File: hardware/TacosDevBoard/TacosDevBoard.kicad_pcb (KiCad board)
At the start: 2 copper layers, 63.6 x 108.1 mm, 12 parts, among them IC2_COMM1 Conn_01x08_Socket, J1 Conn_01x08_Socket, J2 Conn_01x08_Socket, J3 Conn_01x08_Socket, J4 Conn_01x08_Socket, J5 Conn_01x08_Socket, J6 Micro_SD_Card_Det2, J8 Conn_02x17_Odd_Even, J9 Conn_01x10_Pin

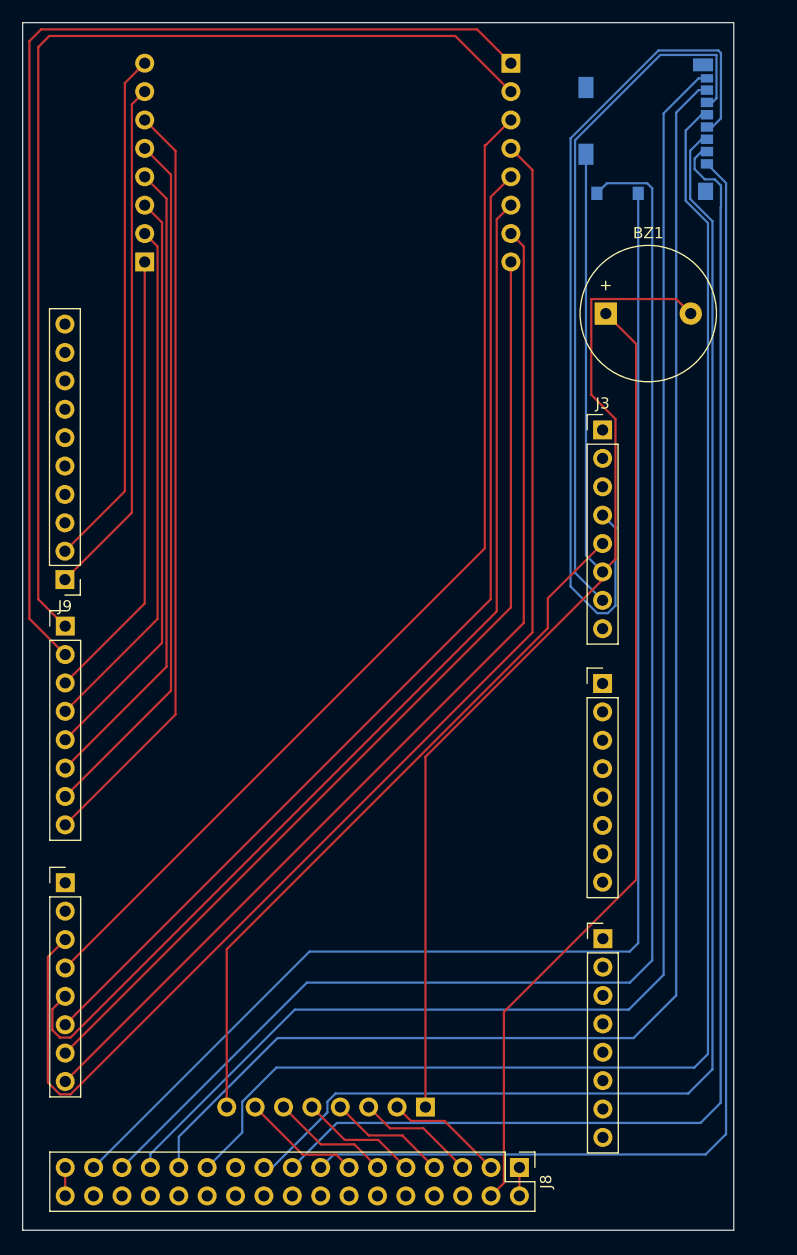
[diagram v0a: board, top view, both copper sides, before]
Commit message: finished dev board rewire
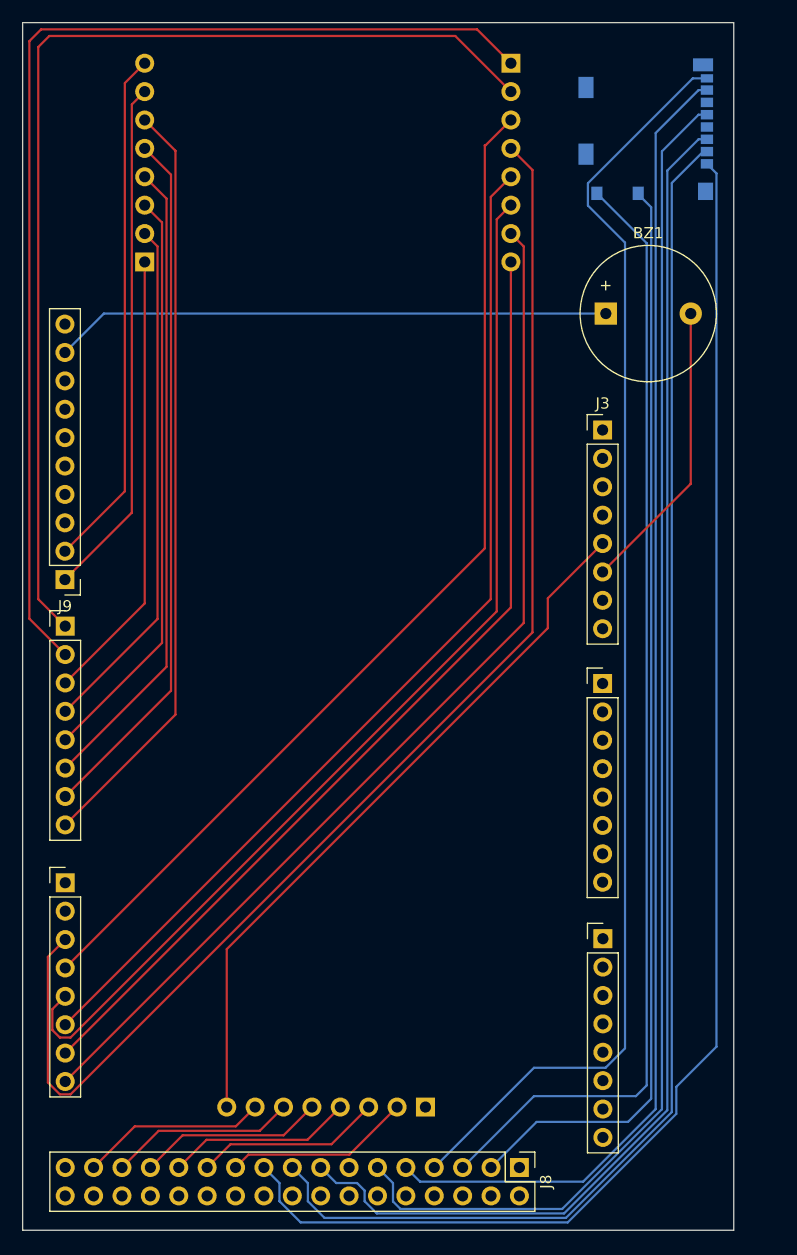
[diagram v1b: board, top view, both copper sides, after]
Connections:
- J8 pad 11: D30 -> SD_CLK
- J8 pad 13: D32 -> unconnected-(J8-Pin_13-Pad13)
- J8 pad 15: SD_DAT2 -> SD_CMD
- J8 pad 19: SD_CMD -> SD_DAT2
- J8 pad 21: unconnected-(J8-Pin_21-Pad21) -> D32
- J8 pad 23: SD_CLK -> D30
- J8 pad 25: SD_DAT0 -> D28
- J8 pad 27: SD_DAT1 -> D26
- J8 pad 29: SD_DET_A -> D24
- J8 pad 3: D22 -> SD_DET_B
- J8 pad 31: SD_DET_B -> D22
- J8 pad 4: D52 -> unconnected-(J8-Pin_4-Pad4)
- J8 pad 5: D24 -> SD_DET_A
- J8 pad 7: D26 -> SD_DAT1
- J8 pad 9: D28 -> SD_DAT0
- J9 pad 9: unconnected-(J9-Pin_9-Pad9) -> D52
- SELECT1 pad 2: D22 -> D32
- SELECT1 pad 3: D24 -> D30
- SELECT1 pad 4: D26 -> D28
- SELECT1 pad 5: D28 -> D26
- SELECT1 pad 6: D30 -> D24
- SELECT1 pad 7: D32 -> D22
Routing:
- net GND: track 130.2 -> 26.4 mm
- net VDD: track 78.2 -> 0.00 mm
- net VSS: track 62.9 -> 0.00 mm
- net D52: track 85.4 -> 49.8 mm
- net SD_DET_A: track 129.7 -> 101.2 mm
- net SD_DET_B: track 124.1 -> 98.4 mm
- net SD_DAT1: track 136.0 -> 114.8 mm
- net SD_DAT0: track 135.1 -> 119.1 mm
- net SD_CLK: track 136.6 -> 122.7 mm
- net D24: track 10.6 -> 16.7 mm
- net D30: track 10.6 -> 16.7 mm
- net D32: track 10.6 -> 16.7 mm
- net D28: track 10.6 -> 16.7 mm
- net D22: track 10.7 -> 16.7 mm
- net D26: track 10.7 -> 16.7 mm
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
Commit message: cleaned up silks
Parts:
- renumbered BZ1 to BZ, IC2_COMM1 to COMM, PWM1 to PWM, SELECT1 to SELECT
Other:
- board text added: "T.A.C.O.S Dev Board"
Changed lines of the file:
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@@
 			(at 0 20.16 0)
 			(layer "F.Fab")
+			(hide yes)
 			(effects
 				(font
@@
 		(descr "Generic Buzzer, D12mm height 9.5mm with RM7.6mm")
 		(tags "buzzer")
-		(property "Reference" "BZ1"
+		(property "Reference" "BZ"
 			(at 3.8 -7.2 0)
 			(layer "F.SilkS")
@@
 			)
 		)
-		(fp_text user "${REFERENCE}"
-			(at 3.8 -4 0)
-			(layer "F.Fab")
-			(effects
-				(font
-					(size 1 1)
-					(thickness 0.15)
-				)
-			)
-		)
 		(pad "1" thru_hole rect
 			(at 0 0)
@@
 			(at 0 -2.38 0)
 			(layer "F.SilkS")
+			(hide yes)
 			(effects
 				(font
@@
 			(at 1.27 -2.38 90)
 			(layer "F.SilkS")
+			(hide yes)
 			(effects
 				(font
@@
 			(at 0 -2.38 0)
 			(layer "F.SilkS")
+			(hide yes)
 			(effects
 				(font
@@
 		(descr "Through hole straight socket strip, 1x08, 2.54mm pitch, single row (from Kicad 4.0.7), script generated")
 		(tags "Through hole socket strip THT 1x08 2.54mm single row")
-		(property "Reference" "PWM1"
-			(at -0.025 -21.336 0)
+		(property "Reference" "PWM"
+			(at 0.0508 -20.3454 0)
 			(layer "B.SilkS")
 			(effects
@@
 		(descr "Through hole straight socket strip, 1x08, 2.54mm pitch, single row (from Kicad 4.0.7), script generated")
 		(tags "Through hole socket strip THT 1x08 2.54mm single row")
-		(property "Reference" "IC2_COMM1"
+		(property "Reference" "COMM"
 			(at 0 2.77 0)
 			(layer "B.SilkS")
@@
 		(descr "Through hole straight socket strip, 1x08, 2.54mm pitch, single row (from Kicad 4.0.7), script generated")
 		(tags "Through hole socket strip THT 1x08 2.54mm single row")
-		(property "Reference" "SELECT1"
+		(property "Reference" "SELECT"
 			(at -2.976 -16.32 0)
 			(layer "B.SilkS")
@@
 		(layer "Edge.Cuts")
 	)
+	(gr_text "T.A.C.O.S Dev Board"
+		(at 157.6832 142.2654 0)
+		(layer "F.SilkS")
+		(effects
+			(font
+				(size 1 1)
+				(thickness 0.1)
+			)
+			(justify left bottom)
+		)
+	)
 	(gr_text "${REFERENCE}"

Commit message: started working on hat detection and selection
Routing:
- net GND: track 26.4 -> 92.3 mm
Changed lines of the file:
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@@
 			(drillshape 0)
 			(scaleselection 1)
-			(outputdirectory "D:/Programming/Aerospace/KiCad/Gerber/")
+			(outputdirectory "DevBoard/")
 		)
 	)
@@
 	)
 	(segment
+		(start 145.2626 131.4958)
+		(end 145.2626 100.1776)
+		(width 0.2)
+		(layer "F.Cu")
+		(net 3)
+	)
+	(segment
+		(start 145.2626 100.1776)
+		(end 161.1122 84.328)
+		(width 0.2)
+		(layer "F.Cu")
+		(net 3)
+	)
+	(segment
 		(start 169 75.729)
 		(end 161.1122 83.6168)
@@
 		(net 3)
 	)
+	(segment
+		(start 161.1122 84.328)
+		(end 161.1122 83.6168)
+		(width 0.2)
+		(layer "F.Cu")
+		(net 3)
+	)
+	(segment
+		(start 170.325 59.175)
+		(end 169 60.5)
+		(width 0.2)
+		(layer "B.Cu")
+		(net 3)
+	)
+	(segment
+		(start 170.325 49.565)
+		(end 170.325 59.175)
+		(width 0.2)
+		(layer "B.Cu")
+		(net 3)
+	)
